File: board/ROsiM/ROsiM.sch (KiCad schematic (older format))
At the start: 93 parts, among them J1 AVR-ISP-6, J2 RS232, J3 Power IN, J4 EXT_ADDR, J5 EXT_D, J6 External ~RESET, J7 External RESET, Q1 2N3904, Q2 2N3906, SW1 SW_Push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

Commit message: Updating for 1.2 PCB
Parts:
- added U21: 74HC04, Package_DIP:DIP-14_W7.62mm, symbol 74xx:74HC04
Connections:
- net labels added: ERST, ~ERST
- wire segments 723 -> 745
- no-connect marks 14 -> 18
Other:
- moved on the sheet: J4, J5, J6, J7, Q1, Q2, R24, R28, R29, R30, U15E

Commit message: Begin designing rev 1.3
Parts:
- removed C4, C5, C6, C7: 1.0uF, Capacitor_THT:CP_Radial_D5.0mm_P2.50mm, symbol Device:CP1_Small
- removed D3: 1N4001, Diode_THT:D_DO-41_SOD81_P10.16mm_Horizontal, symbol Diode:1N4001
- removed J2: RS232, Connector_Dsub:DSUB-9_Female_Horizontal_P2.77x2.84mm_EdgePinOffset4.94mm_Housed_MountingHolesOffset7.48mm, symbol Connector:DB9_Female_MountingHoles
- removed J3: Power IN, Connector_BarrelJack:BarrelJack_Horizontal, symbol Connector:Conn_Coaxial_Power
- removed SW2: Power, EproSim:Slide_Switch, symbol Switch:SW_SPST
- removed U6: MAX232, Package_DIP:DIP-16_W7.62mm, symbol Interface_UART:MAX232
- removed U7: L7805, Package_TO_SOT_THT:TO-220-3_Horizontal_TabDown, symbol Regulator_Linear:L7805
- added D3: TX, LED_THT:LED_D2.0mm_W4.8mm_H2.5mm_FlatTop, symbol Device:LED_Small
- added D4: RX, LED_THT:LED_D2.0mm_W4.8mm_H2.5mm_FlatTop, symbol Device:LED_Small
- added F1: 500mA, Fuse:Fuse_1206_3216Metric, symbol Device:Polyfuse_Small
- added J2: USB_B, Connector_USB:USB_B_Lumberg_2411_02_Horizontal, symbol Connector:USB_B
- added JP1: VCCIO sel, Jumper:SolderJumper-2_P1.3mm_Open_RoundedPad1.0x1.5mm, symbol Device:Jumper_NO_Small
- added R31, R32: 470, Resistor_THT:R_Axial_DIN0204_L3.6mm_D1.6mm_P7.62mm_Horizontal, symbol Device:R_Small
- added U6: FT232RL, Package_SO:SSOP-28_5.3x10.2mm_P0.65mm, symbol Interface_USB:FT232RL
- C15: value 0.22uF -> 10uF
- R17: value 1.2K -> 1K
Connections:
- net labels added: +3.3V
- net labels removed: +12V, RECT_V12, RS232-DTR, RS232-RX, RS232-TX, SW_12V
- wire segments 745 -> 736
- no-connect marks 18 -> 13
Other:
- moved on the sheet: C14, C15, C3, D2, R17

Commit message: Updated readme and 1.3 pcb
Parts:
- added C29: 100nF, Capacitor_THT:C_Disc_D3.4mm_W2.1mm_P2.50mm, symbol Device:C_Small
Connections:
- wire segments 736 -> 737
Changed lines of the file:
@@
 	2750 7150 3500 7150
 Connection ~ 3500 7150
-Text Label 5050 5750 2    50   ~ 0
+Text Label 5450 5750 2    50   ~ 0
 ~RESET
-Wire Wire Line
-	4500 5750 5050 5750
 Wire Wire Line
 	4500 5350 5050 5350
@@
 Connection ~ 1550 8950
 Connection ~ 2150 9150
+$Comp
+L Device:C_Small C29
+U 1 1 633732E4
+P 4850 5750
+F 0 "C29" V 4950 5850 50  0000 C CNN
+F 1 "100nF" V 4950 5600 50  0000 C CNN
+F 2 "Capacitor_THT:C_Disc_D3.4mm_W2.1mm_P2.50mm" H 4850 5750 50  0001 C CNN
+F 3 "~" H 4850 5750 50  0001 C CNN
+	1    4850 5750
+	0    -1   -1   0
+$EndComp
+Wire Wire Line
+	4500 5750 4750 5750
+Wire Wire Line
+	4950 5750 5450 5750
 $EndSCHEMATC

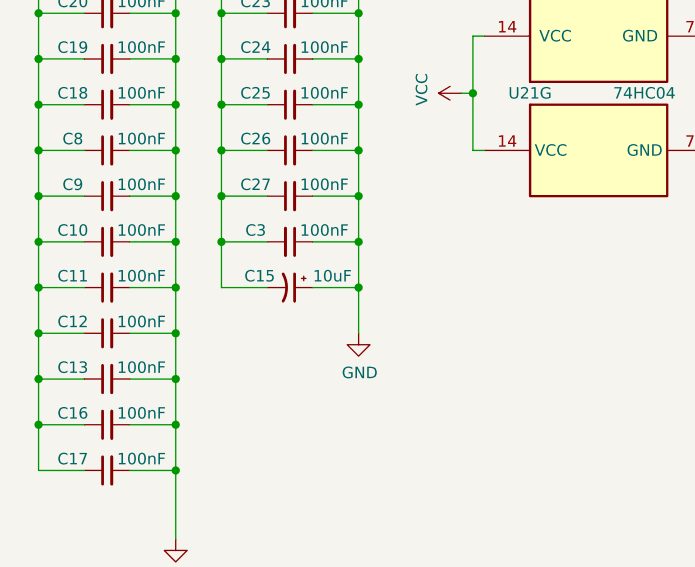
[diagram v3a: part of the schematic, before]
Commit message: Whoops, a cap was inverted
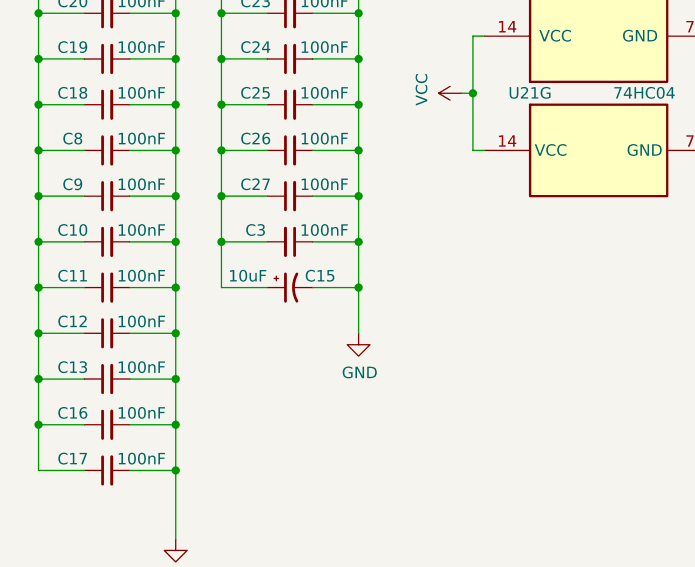
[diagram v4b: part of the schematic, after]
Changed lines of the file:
@@
 F 3 "~" H 1850 9150 50  0001 C CNN
 	1    1850 9150
-	0    1    1    0
+	0    -1   1    0
 $EndComp
 Wire Wire Line

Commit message: Update the schematics
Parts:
- U1: value ATmega8A-PU -> ATmega328P
- Y1: value 8Mhz -> 20Mhz
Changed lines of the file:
@@
 P 2300 2500
 F 0 "U1" H 1850 3850 50  0000 C CNN
-F 1 "ATmega8A-PU" H 2750 3850 50  0000 C CNN
+F 1 "ATmega328P" H 2750 3850 50  0000 C CNN
 F 2 "Package_DIP:DIP-28_W7.62mm" H 2300 2500 50  0001 C CIN
 F 3 "http://ww1.microchip.com/downloads/en/DeviceDoc/Microchip%208bit%20mcu%20AVR%20ATmega8A%20data%20sheet%2040001974A.pdf" H 2300 2500 50  0001 C CNN
@@
 P 5350 2550
 F 0 "Y1" V 5400 2750 50  0000 R CNN
-F 1 "8Mhz" V 5300 2850 50  0000 R CNN
+F 1 "20Mhz" V 5300 2850 50  0000 R CNN
 F 2 "Crystal:Crystal_HC49-U_Vertical" H 5350 2550 50  0001 C CNN
 F 3 "~" H 5350 2550 50  0001 C CNN

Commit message: Update ROsiM design
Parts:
- removed JP1: VCCIO sel, Jumper:SolderJumper-2_P1.3mm_Open_RoundedPad1.0x1.5mm, symbol Device:Jumper_NO_Small
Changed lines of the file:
@@
 Title "ROsiM"
 Date ""
-Rev "1.3"
+Rev "1.4"
 Comp ""
 Comment1 ""
@@
 U 1 1 5E8D0A0C
 P 2600 4550
-F 0 "C14" V 2700 4650 50  0000 C CNN
-F 1 "100nF" V 2700 4400 50  0000 C CNN
+F 0 "C14" V 2750 4550 50  0000 C CNN
+F 1 "100nF" V 2500 4550 50  0000 C CNN
 F 2 "Capacitor_THT:C_Disc_D3.4mm_W2.1mm_P2.50mm" H 2600 4550 50  0001 C CNN
 F 3 "~" H 2600 4550 50  0001 C CNN
@@
 $EndComp
 Wire Wire Line
-	3800 5050 3800 4900
-$Comp
-L Device:Jumper_NO_Small JP1
-U 1 1 60BD9B01
-P 3600 4850
-F 0 "JP1" V 3650 4750 50  0000 R CNN
-F 1 "VCCIO sel" V 3550 4750 50  0000 R CNN
-F 2 "Jumper:SolderJumper-2_P1.3mm_Open_RoundedPad1.0x1.5mm" H 3600 4850 50  0001 C CNN
-F 3 "~" H 3600 4850 50  0001 C CNN
-	1    3600 4850
-	0    1    -1   0
-$EndComp
-Wire Wire Line
-	3600 5050 3600 4950
+	3800 5050 3800 4950
 Wire Wire Line
 	2900 5350 2800 5350
 Wire Wire Line
 	2800 5350 2800 4550
-Wire Wire Line
-	2800 4550 3600 4550
-Wire Wire Line
-	3600 4550 3600 4750
 $Comp
 L power:+3.3V #PWR0116
 U 1 1 60EB64AB
-P 3600 4450
-F 0 "#PWR0116" H 3600 4300 50  0001 C CNN
-F 1 "+3.3V" H 3615 4623 50  0000 C CNN
-F 2 "" H 3600 4450 50  0001 C CNN
-F 3 "" H 3600 4450 50  0001 C CNN
-	1    3600 4450
+P 2800 4450
+F 0 "#PWR0116" H 2800 4300 50  0001 C CNN
+F 1 "+3.3V" H 2815 4623 50  0000 C CNN
+F 2 "" H 2800 4450 50  0001 C CNN
+F 3 "" H 2800 4450 50  0001 C CNN
+	1    2800 4450
 	1    0    0    -1
 $EndComp
 Wire Wire Line
-	3600 4450 3600 4550
-Connection ~ 3600 4550
-Wire Wire Line
 	2700 4550 2800 4550
 Connection ~ 2800 4550
@@
 Wire Wire Line
 	4950 5750 5450 5750
+Wire Wire Line
+	2800 4550 2800 4450
+Wire Wire Line
+	3800 4950 3600 4950
+Wire Wire Line
+	3600 4950 3600 5050
+Connection ~ 3800 4950
+Wire Wire Line
+	3800 4950 3800 4900
 $EndSCHEMATC

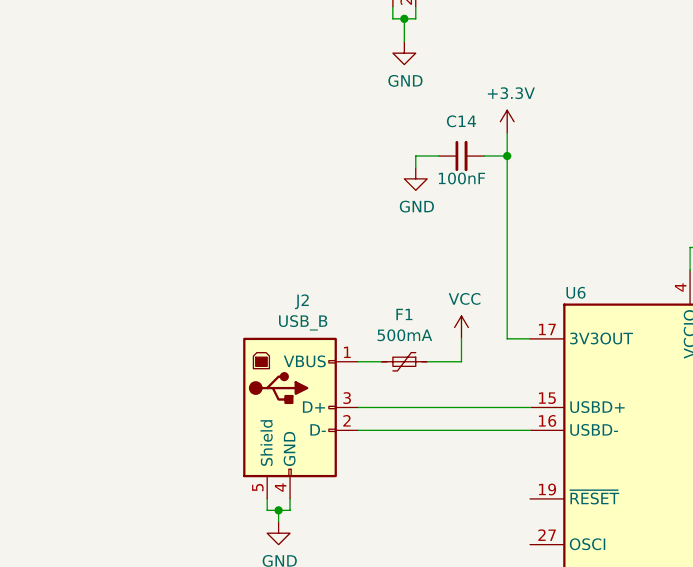
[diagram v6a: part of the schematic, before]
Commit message: Added schottky diode on USB +5v input
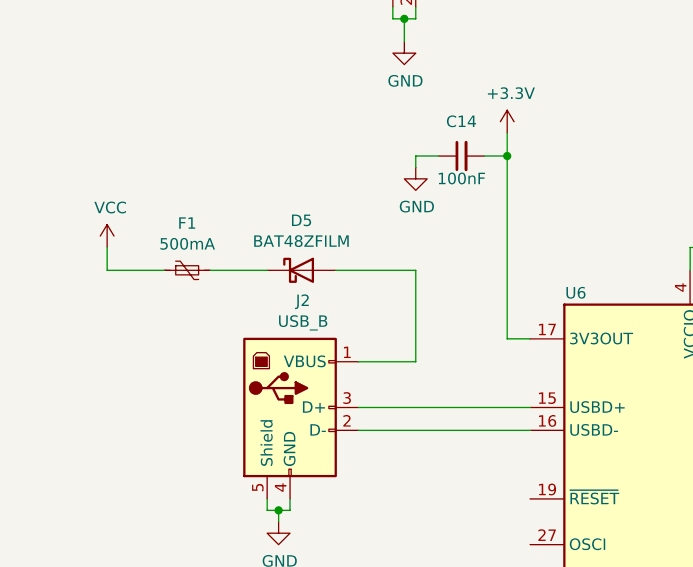
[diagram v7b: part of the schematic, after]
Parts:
- added D5: BAT48ZFILM, Diode_SMD:D_SOD-123, symbol Diode:BAT48ZFILM
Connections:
- net at J2.1 (VBUS): now also D5.2 (A); no longer F1.2
- new net: D5.1 (K), F1.2
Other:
- moved on the sheet: F1
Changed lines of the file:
@@
 $EndComp
 Wire Wire Line
-	2600 5450 2600 5350
-Wire Wire Line
-	2450 5450 2600 5450
+	1050 5050 1050 4950
 $Comp
 L power:VCC #PWR0120
 U 1 1 60451FCD
-P 2600 5350
-F 0 "#PWR0120" H 2600 5200 50  0001 C CNN
-F 1 "VCC" H 2615 5523 50  0000 C CNN
-F 2 "" H 2600 5350 50  0001 C CNN
-F 3 "" H 2600 5350 50  0001 C CNN
-	1    2600 5350
-	1    0    0    -1
-$EndComp
-Wire Wire Line
-	2150 5450 2250 5450
+P 1050 4950
+F 0 "#PWR0120" H 1050 4800 50  0001 C CNN
+F 1 "VCC" H 1065 5123 50  0000 C CNN
+F 2 "" H 1050 4950 50  0001 C CNN
+F 3 "" H 1050 4950 50  0001 C CNN
+	1    1050 4950
+	1    0    0    -1
+$EndComp
 Wire Wire Line
 	1800 6100 1850 6100
@@
 L Device:Polyfuse_Small F1
 U 1 1 6000F02B
-P 2350 5450
-F 0 "F1" V 2145 5450 50  0000 C CNN
-F 1 "500mA" V 2236 5450 50  0000 C CNN
-F 2 "Fuse:Fuse_1206_3216Metric" H 2400 5250 50  0001 L CNN
-F 3 "~" H 2350 5450 50  0001 C CNN
-	1    2350 5450
-	0    1    1    0
+P 1400 5050
+F 0 "F1" V 1195 5050 50  0000 C CNN
+F 1 "500mA" V 1286 5050 50  0000 C CNN
+F 2 "Fuse:Fuse_1206_3216Metric" H 1450 4850 50  0001 L CNN
+F 3 "~" H 1400 5050 50  0001 C CNN
+	1    1400 5050
+	0    -1   1    0
 $EndComp
 $Comp
@@
 Wire Wire Line
 	3800 4950 3800 4900
+$Comp
+L Diode:BAT48ZFILM D5
+U 1 1 60152895
+P 1900 5050
+F 0 "D5" H 1900 5267 50  0000 C CNN
+F 1 "BAT48ZFILM" H 1900 5176 50  0000 C CNN
+F 2 "Diode_SMD:D_SOD-123" H 1900 4875 50  0001 C CNN
+F 3 "www.st.com/resource/en/datasheet/bat48.pdf" H 1900 5050 50  0001 C CNN
+	1    1900 5050
+	1    0    0    -1
+$EndComp
+Wire Wire Line
+	2400 5450 2400 5050
+Wire Wire Line
+	2400 5050 2050 5050
+Wire Wire Line
+	2150 5450 2400 5450
+Wire Wire Line
+	1750 5050 1500 5050
+Wire Wire Line
+	1300 5050 1050 5050
 $EndSCHEMATC

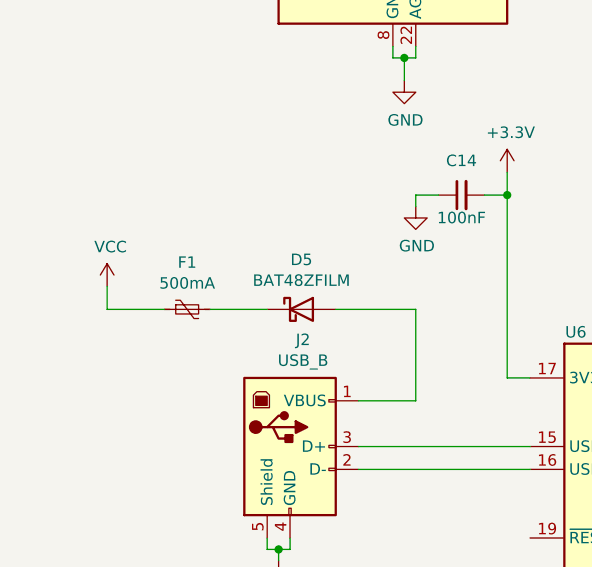
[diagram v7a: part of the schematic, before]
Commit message: Lower specification of F1 to 200mA, to stay under BAT48 max current
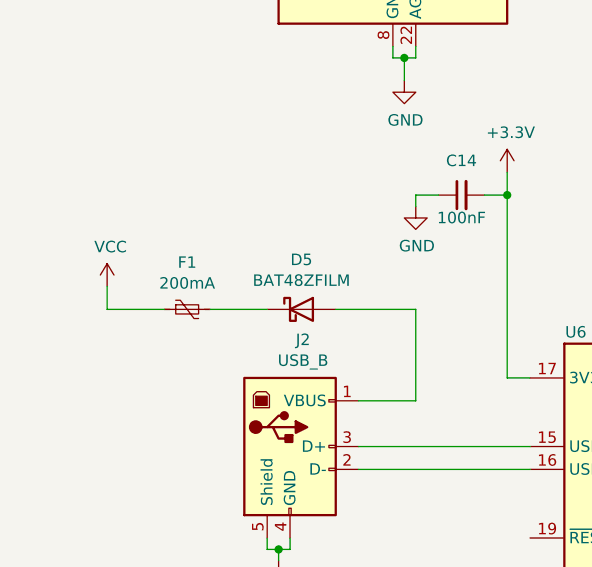
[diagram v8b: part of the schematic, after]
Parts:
- F1: value 500mA -> 200mA
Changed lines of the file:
@@
 P 1400 5050
 F 0 "F1" V 1195 5050 50  0000 C CNN
-F 1 "500mA" V 1286 5050 50  0000 C CNN
+F 1 "200mA" V 1286 5050 50  0000 C CNN
 F 2 "Fuse:Fuse_1206_3216Metric" H 1450 4850 50  0001 L CNN
 F 3 "~" H 1400 5050 50  0001 C CNN
